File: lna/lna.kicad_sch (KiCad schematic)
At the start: 18 parts, among them J1 Conn_Coaxial, J2 V5-GND, J3 Conn_Coaxial, U1 PGA-103+

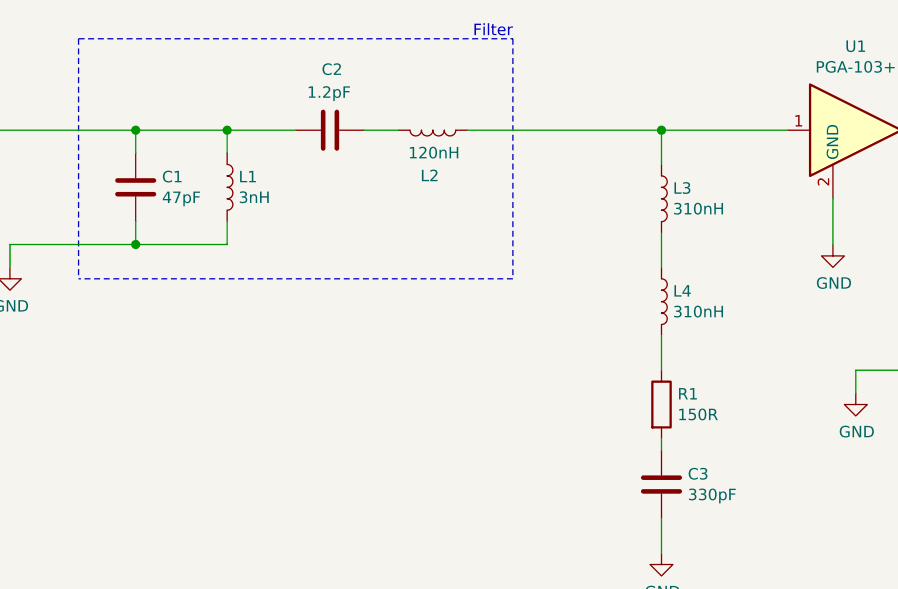
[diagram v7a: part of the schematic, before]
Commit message: Add proper values of components & update readme
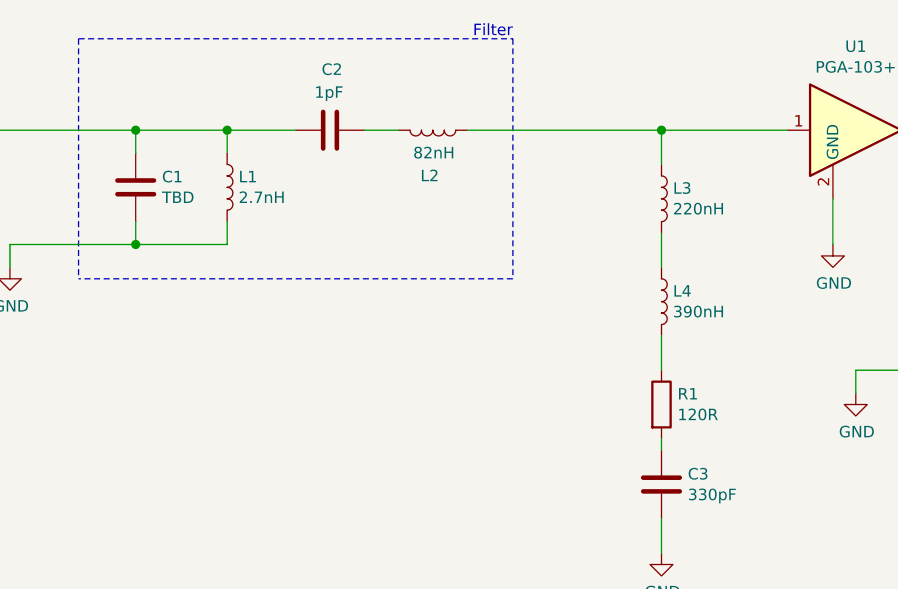
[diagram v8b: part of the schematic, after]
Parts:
- C1: value 47pF -> TBD
- C2: value 1.2pF -> 1pF
- L1: value 3nH -> 2.7nH
- L2: value 120nH -> 82nH
- L3: value 310nH -> 220nH
- L4: value 310nH -> 390nH
- R1: value 150R -> 120R
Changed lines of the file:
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@@
       (effects (font (size 1.27 1.27)) (justify left))
     )
-    (property "Value" "3nH" (id 1) (at 63.5 48.139 0)
+    (property "Value" "2.7nH" (id 1) (at 63.5 48.139 0)
       (effects (font (size 1.27 1.27)) (justify left))
     )
@@
       (effects (font (size 1.27 1.27)) (justify left))
     )
-    (property "Value" "120nH" (id 1) (at 85.211 43.18 90))
+    (property "Value" "82nH" (id 1) (at 85.211 43.18 90))
     (property "Footprint" "Inductor_SMD:L_0805_2012Metric" (id 2) (at 85.09 40.64 0)
       (effects (font (size 1.27 1.27)) hide)
@@
       (effects (font (size 1.27 1.27)) (justify left))
     )
-    (property "Value" "310nH" (id 1) (at 111.76 49.409 0)
+    (property "Value" "220nH" (id 1) (at 111.76 49.409 0)
       (effects (font (size 1.27 1.27)) (justify left))
     )
@@
       (effects (font (size 1.27 1.27)) (justify left))
     )
-    (property "Value" "310nH" (id 1) (at 111.76 60.839 0)
+    (property "Value" "390nH" (id 1) (at 111.76 60.839 0)
       (effects (font (size 1.27 1.27)) (justify left))
     )
@@
       (effects (font (size 1.27 1.27)) (justify left))
     )
-    (property "Value" "150R" (id 1) (at 112.268 72.269 0)
+    (property "Value" "120R" (id 1) (at 112.268 72.269 0)
       (effects (font (size 1.27 1.27)) (justify left))
     )
@@
       (effects (font (size 1.27 1.27)) (justify left))
     )
-    (property "Value" "47pF" (id 1) (at 54.991 48.139 0)
+    (property "Value" "TBD" (id 1) (at 54.991 48.139 0)
       (effects (font (size 1.27 1.27)) (justify left))
     )
@@
       (effects (font (size 1.27 1.27)) (justify left))
     )
-    (property "Value" "1.2pF" (id 1) (at 73.539 36.449 90))
+    (property "Value" "1pF" (id 1) (at 73.539 36.449 90))
     (property "Footprint" "Capacitor_SMD:C_0603_1608Metric" (id 2) (at 77.47 39.6748 0)
       (effects (font (size 1.27 1.27)) hide)
@@
     )
     (path "/e3613cca-fb62-4c1e-9e92-3c0f2f895470"
-      (reference "C1") (unit 1) (value "47pF") (footprint "Capacitor_SMD:C_0603_1608Metric")
+      (reference "C1") (unit 1) (value "TBD") (footprint "Capacitor_SMD:C_0603_1608Metric")
     )
     (path "/4de7368e-cf8f-457d-894b-7cde015e5ae4"
-      (reference "C2") (unit 1) (value "1.2pF") (footprint "Capacitor_SMD:C_0603_1608Metric")
+      (reference "C2") (unit 1) (value "1pF") (footprint "Capacitor_SMD:C_0603_1608Metric")
     )
     (path "/9236375b-8363-44f6-bfdd-a5740e45b8df"
@@
     )
     (path "/5c96d87d-8e59-4bd2-bdb2-f94bde9c9bde"
-      (reference "L1") (unit 1) (value "3nH") (footprint "Inductor_SMD:L_0805_2012Metric")
+      (reference "L1") (unit 1) (value "2.7nH") (footprint "Inductor_SMD:L_0805_2012Metric")
     )
     (path "/d14bdfd7-723c-44eb-a88a-d24bcf6f1d60"
-      (reference "L2") (unit 1) (value "120nH") (footprint "Inductor_SMD:L_0805_2012Metric")
+      (reference "L2") (unit 1) (value "82nH") (footprint "Inductor_SMD:L_0805_2012Metric")
     )
     (path "/f12b8427-df59-4712-8d32-ccaa47282c60"
-      (reference "L3") (unit 1) (value "310nH") (footprint "Inductor_SMD:L_0805_2012Metric")
+      (reference "L3") (unit 1) (value "220nH") (footprint "Inductor_SMD:L_0805_2012Metric")
     )
     (path "/fae398ff-66f1-43b9-aeae-6cc366615582"
-      (reference "L4") (unit 1) (value "310nH") (footprint "Inductor_SMD:L_0805_2012Metric")
+      (reference "L4") (unit 1) (value "390nH") (footprint "Inductor_SMD:L_0805_2012Metric")
     )
     (path "/26f751ea-b1d1-4718-ba11-fc72fe07288b"
@@
     )
     (path "/3e341f7d-e5e1-4dc3-826f-31adc6ec84d8"
-      (reference "R1") (unit 1) (value "150R") (footprint "Resistor_SMD:R_0603_1608Metric")
+      (reference "R1") (unit 1) (value "120R") (footprint "Resistor_SMD:R_0603_1608Metric")
     )
     (path "/f1b04b91-1dfc-41e6-a27c-3632286e43ae"
